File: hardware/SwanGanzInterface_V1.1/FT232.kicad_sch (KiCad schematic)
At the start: 0 parts

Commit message: Hooked up MSP
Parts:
- added C25: C, symbol Device:C
- added U6: FT232RL, SGI_FootprintsLib:FT232RL, symbol SGI_SymbolLib:FT232RL
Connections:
- new net FT_+3V3: C25.1, U6.17 (3V3OUT), U6.4 (VCCIO)
- new net GND: C25.2, U6.18 (GND_2), U6.21 (GND_3), U6.25 (AGND), U6.7 (GND_1)

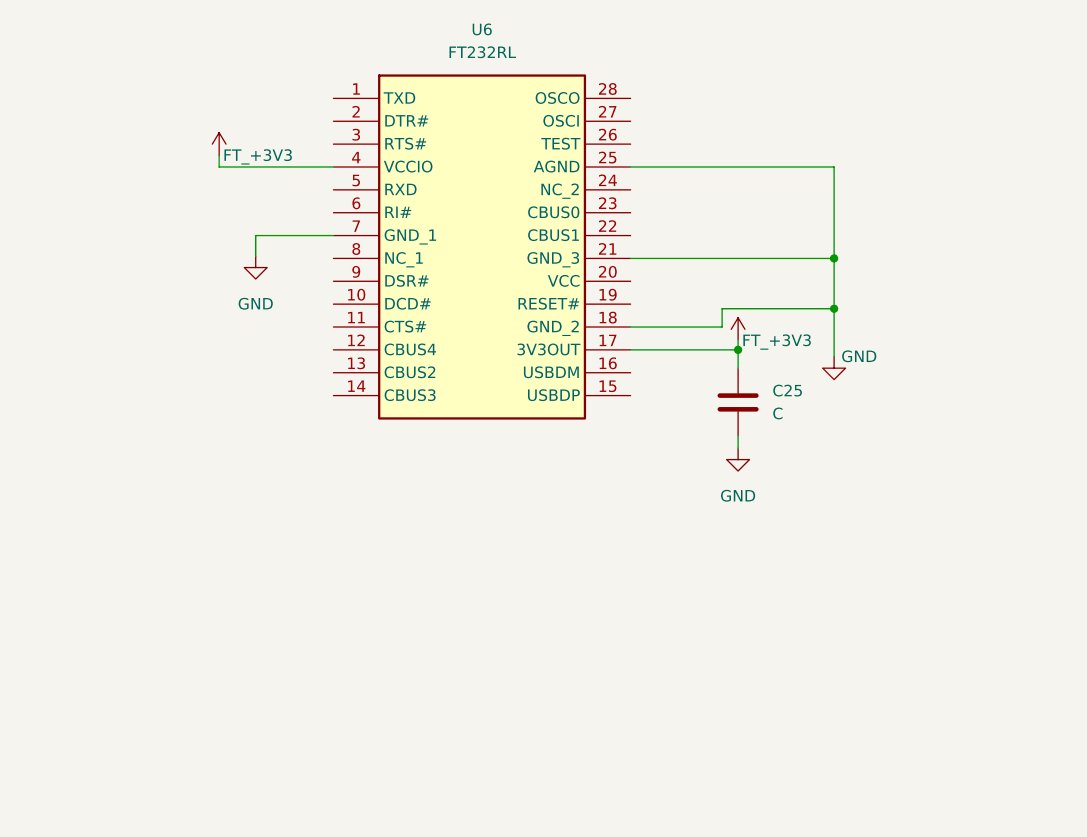
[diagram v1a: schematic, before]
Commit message: Worked on FT232R circuit - RTS, CTS etc
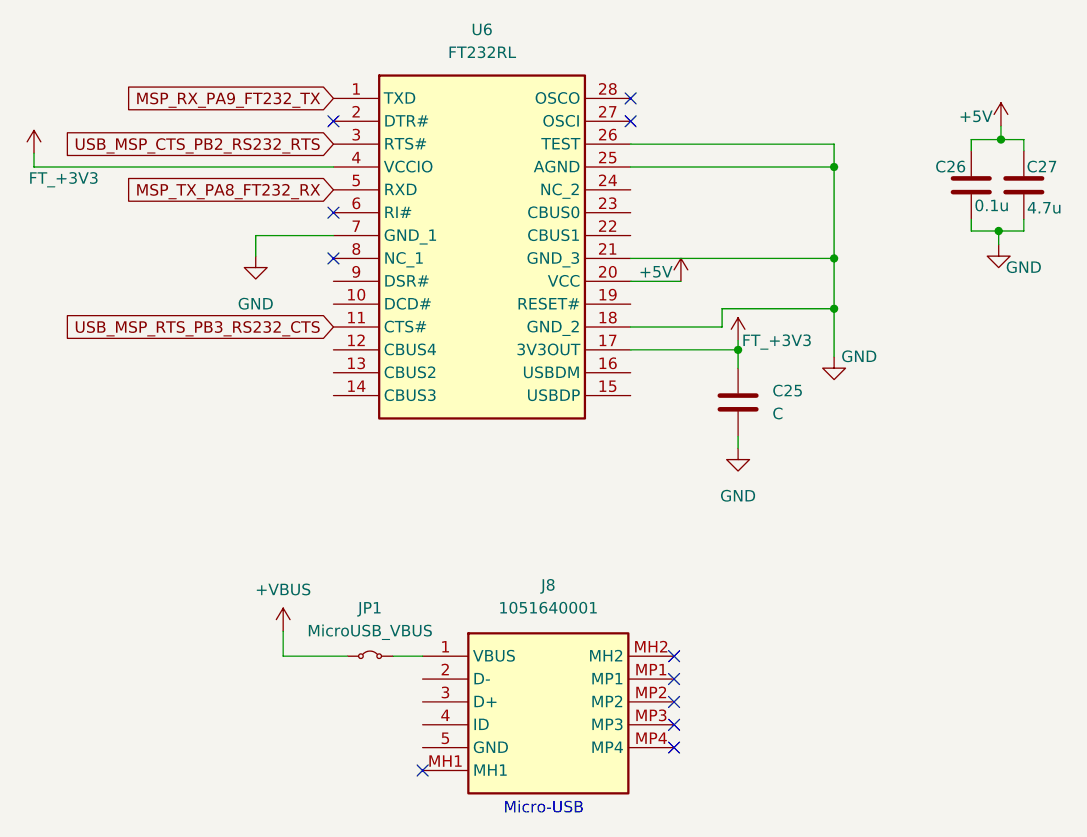
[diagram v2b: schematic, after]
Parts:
- added C26: 0.1u, symbol Device:C
- added C27: 4.7u, symbol Device:C
- added J8: 1051640001, SGI_FootprintsLib:1051640001, symbol SGI_SymbolLib:1051640001
- added JP1: MicroUSB_VBUS, SGI_FootprintsLib:PinHeader_1x02_P2.54mm_Vertical, symbol Jumper:Jumper_2_Small_Bridged
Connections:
- net GND: now also U6.26 (TEST), C26.1, C27.1
- net MSP_RX_PA9_FT232_TX: now reaches U6.1 (TXD)
- net USB_MSP_RTS_PB3_RS232_CTS: now reaches U6.11 (CTS#)
- net +5V: now reaches U6.20 (VCC)
- net +5V: now also C26.2, C27.2
- net USB_MSP_CTS_PB2_RS232_RTS: now reaches U6.3 (RTS#)
- net MSP_TX_PA8_FT232_RX: now reaches U6.5 (RXD)
- new net: J8.1 (VBUS), JP1.2 (B)
- new net +VBUS: JP1.1 (A)
- no-connect marks 0 -> 11
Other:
- note added: "Micro-USB"

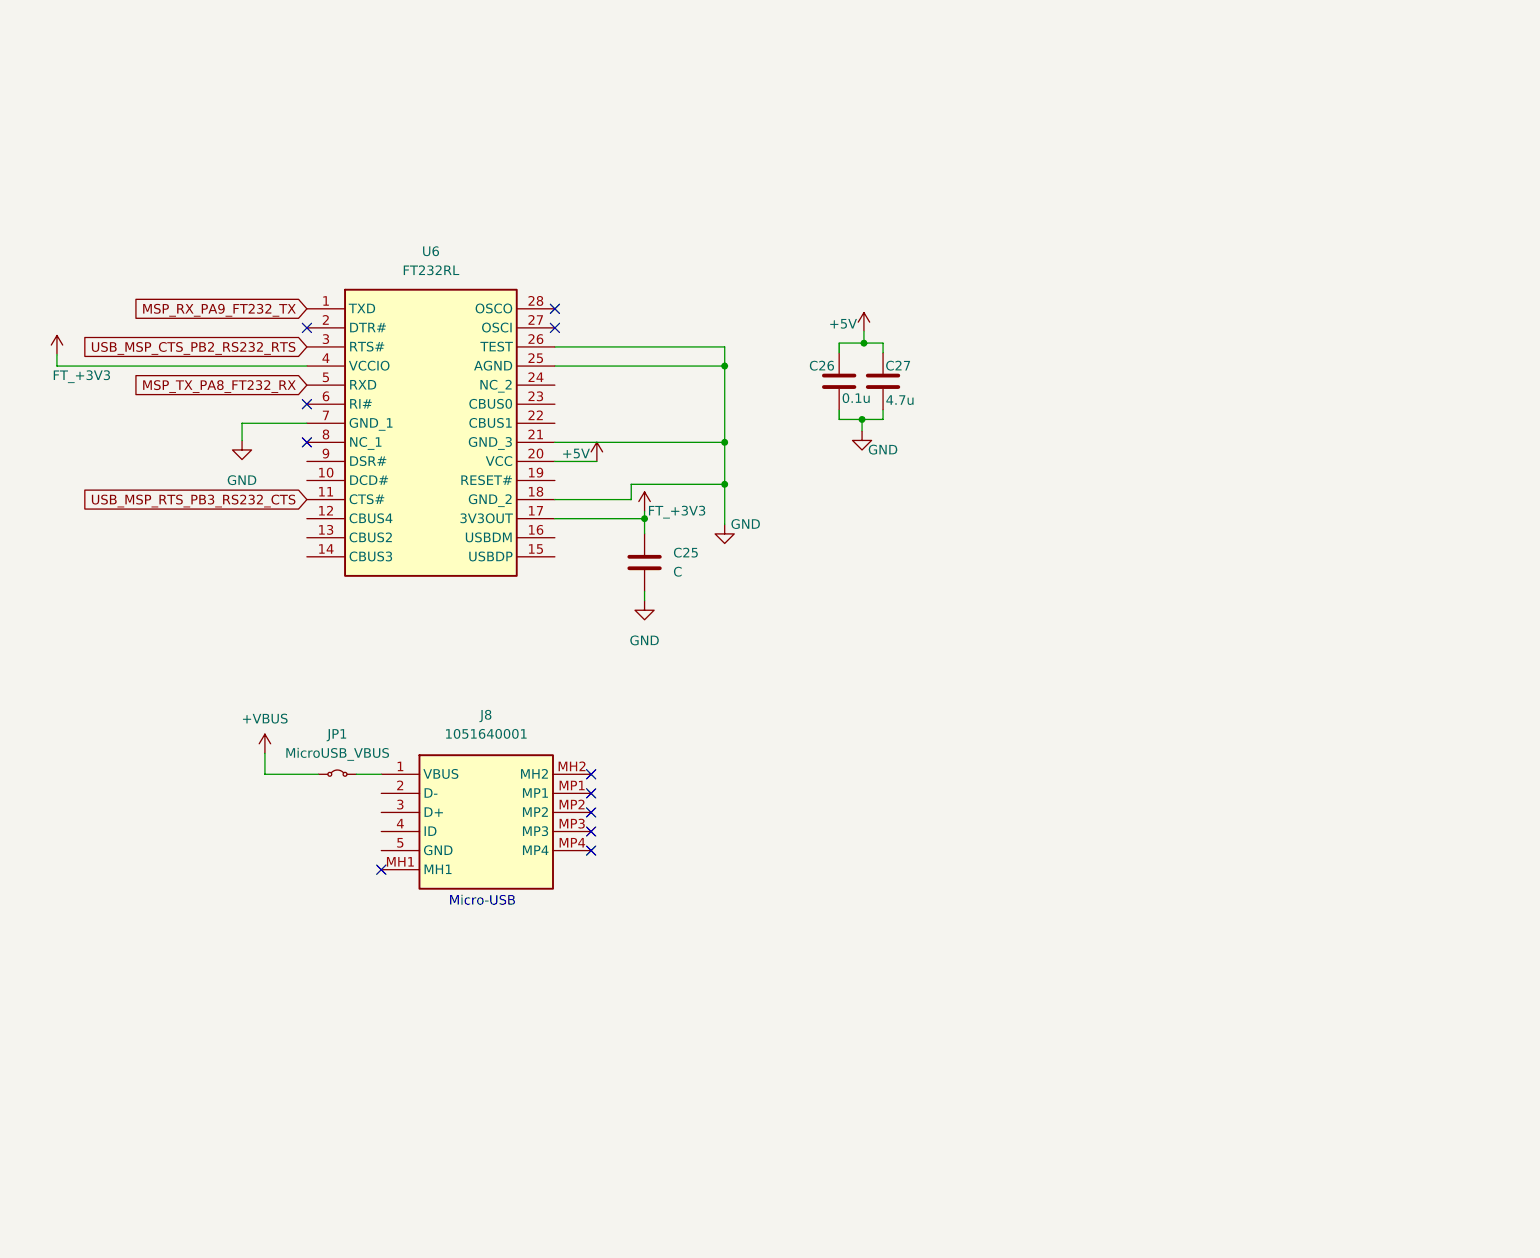
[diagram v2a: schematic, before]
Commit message: Added crystal loading caps
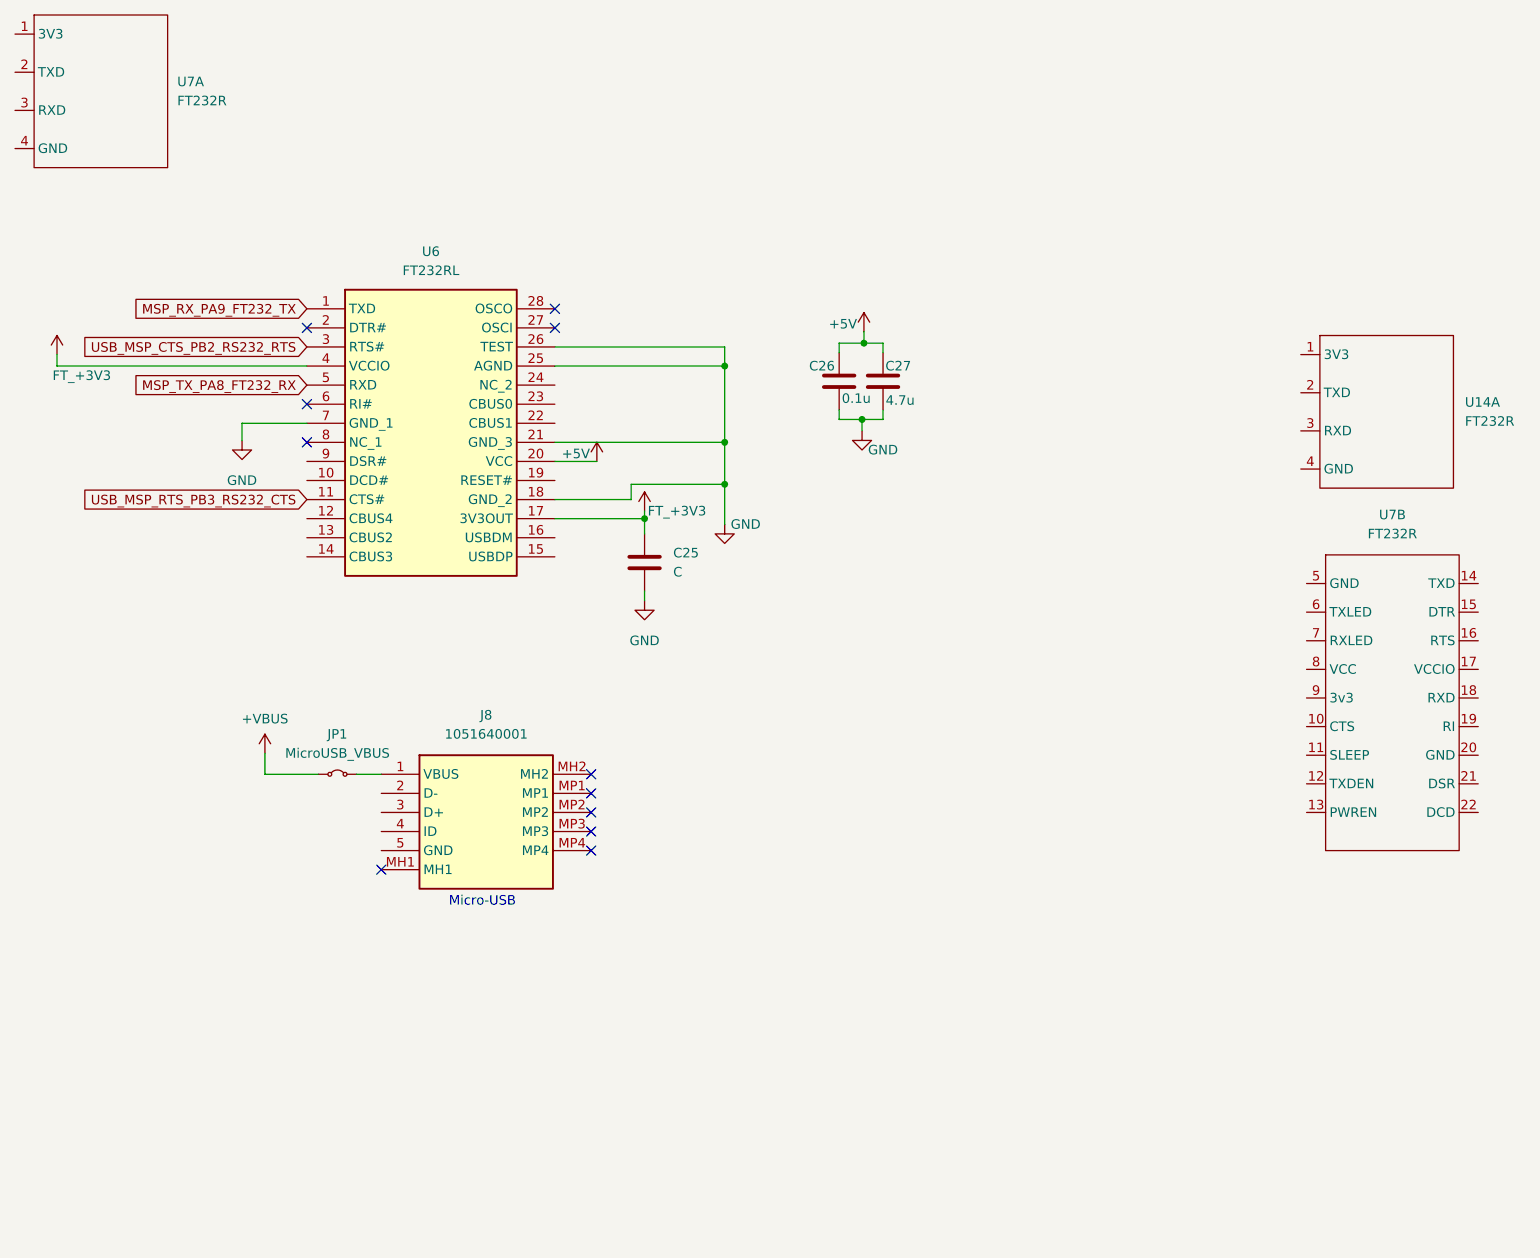
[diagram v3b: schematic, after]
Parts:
- added U14, U7: FT232R, SGI_FootprintsLib:FT232R-Breakout, symbol SGI_SymbolLib:FT232R-Breakout
- U6: Arrow Part Number FT232RL -> FT232RNL; Manufacturer_Part_Number FT232RL -> FT232RNL

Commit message: Added work on FT232, added transmit and receieve leds
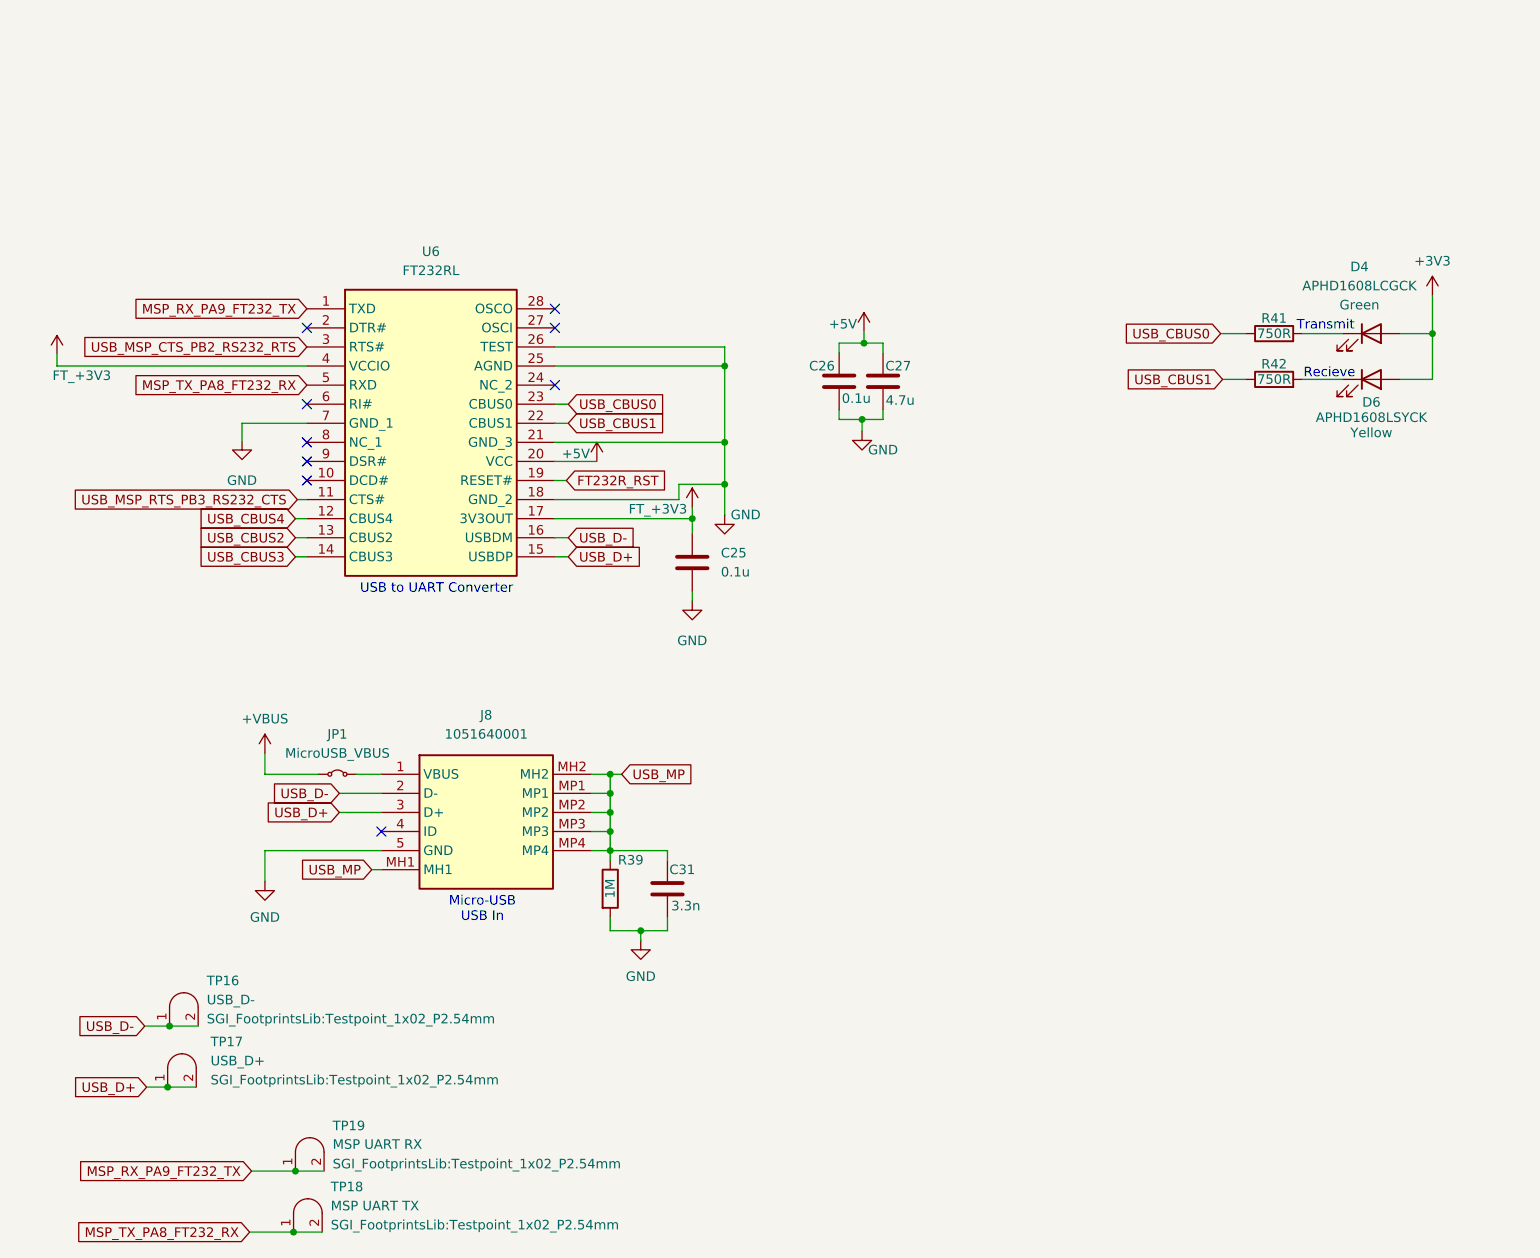
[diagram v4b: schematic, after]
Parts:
- removed U14, U7: FT232R, SGI_FootprintsLib:FT232R-Breakout, symbol SGI_SymbolLib:FT232R-Breakout
- added C31: 3.3n, symbol Device:C
- added D4: APHD1608LCGCK, Diode_SMD:D_0603_1608Metric, symbol SGI_SymbolLib:APHD1608LCGCK
- added D6: APHD1608LSYCK, Diode_SMD:D_0603_1608Metric, symbol SGI_SymbolLib:APHD1608LSYCK
- added R39: 1M, symbol Device:R
- added R41, R42: 750R, symbol Device:R
- added TP16: USB_D-, SGI_FootprintsLib:Testpoint_1x02_P2.54mm, symbol SGI_SymbolLib:Testpoint
- added TP17: USB_D+, SGI_FootprintsLib:Testpoint_1x02_P2.54mm, symbol SGI_SymbolLib:Testpoint
- added TP18: MSP UART TX, SGI_FootprintsLib:Testpoint_1x02_P2.54mm, symbol SGI_SymbolLib:Testpoint
- added TP19: MSP UART RX, SGI_FootprintsLib:Testpoint_1x02_P2.54mm, symbol SGI_SymbolLib:Testpoint
- C25: value C -> 0.1u
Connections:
- net GND: now also J8.5 (GND), C31.2, R39.2
- net MSP_RX_PA9_FT232_TX: now also TP19.1 (A), TP19.2 (B)
- net MSP_TX_PA8_FT232_RX: now also TP18.1 (A), TP18.2 (B)
- net USB_CBUS4: now reaches U6.12 (CBUS4)
- net USB_CBUS2: now reaches U6.13 (CBUS2)
- net USB_CBUS3: now reaches U6.14 (CBUS3)
- net USB_D+: now reaches U6.15 (USBDP)
- net USB_D+: now also J8.3 (D+), TP17.1 (A), TP17.2 (B)
- net USB_D-: now reaches U6.16 (USBDM)
- net USB_D-: now also J8.2 (D-), TP16.1 (A), TP16.2 (B)
- net FT232R_RST: now reaches U6.19 (RESET#)
- net USB_CBUS1: now reaches U6.22 (CBUS1)
- net USB_CBUS1: now also R42.1
- net USB_CBUS0: now reaches U6.23 (CBUS0)
- net USB_CBUS0: now also R41.1
- net USB_MP: now reaches J8.MH1
- net USB_MP: now also J8.MH2, J8.MP1, J8.MP2, J8.MP3, J8.MP4, C31.1, R39.1
- new net: D6.1 (K), R42.2
- new net: D4.1 (K), R41.2
- new net +3V3: D4.2 (A), D6.2 (A)
- no-connect marks 11 -> 9
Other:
- note added: "Recieve"
- note added: "Transmit"
- note added: "USB In"
- note added: "USB to UART Converter"
- moved on the sheet: C25
